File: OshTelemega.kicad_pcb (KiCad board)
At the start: 4 copper layers, 30 x 80 mm, 157 parts, among them J1 TAGCONNECT, J10 SERVOS, J2 Conn_01x02, J3 SMA_Edgelaunch, J4 USB_C_Receptacle_USB2.0_16P, J5 UFL, J6 RIGHT, J7 LEFT, J8 BATT, J9 Conn_02x05_Counter_Clockwise, Q1 SiA449DJ, Q2 AO3400A, Q3 SiA449DJ, Q4 SiA449DJ, U1 STM32L151VCTx, U10 MMC5983MA, U11 TSM200N03, U12 LM293QT, U13 LM293QT, U14 TSM200N03, U15 LM293QT, U16 TSM200N03, U17 MCP73831-2-OT, U18 TC2185-3.3VxCTTR, U19 W25Q64JVXGIQ, U2 WE-TVS-82400102, U21 SN74LVC1G80QDCKTQ1, U3 ADXL375, U4 MS5607-02BA, U5 MAX-M10S, U6 MCP130-xxxxTT, U7 DRV5012AEDMRR, U8 CC1200, U9 BMI088, X2 ECS-160-8-36Q-AES-TR1, Y1 ABM8W-40.0000MHZ

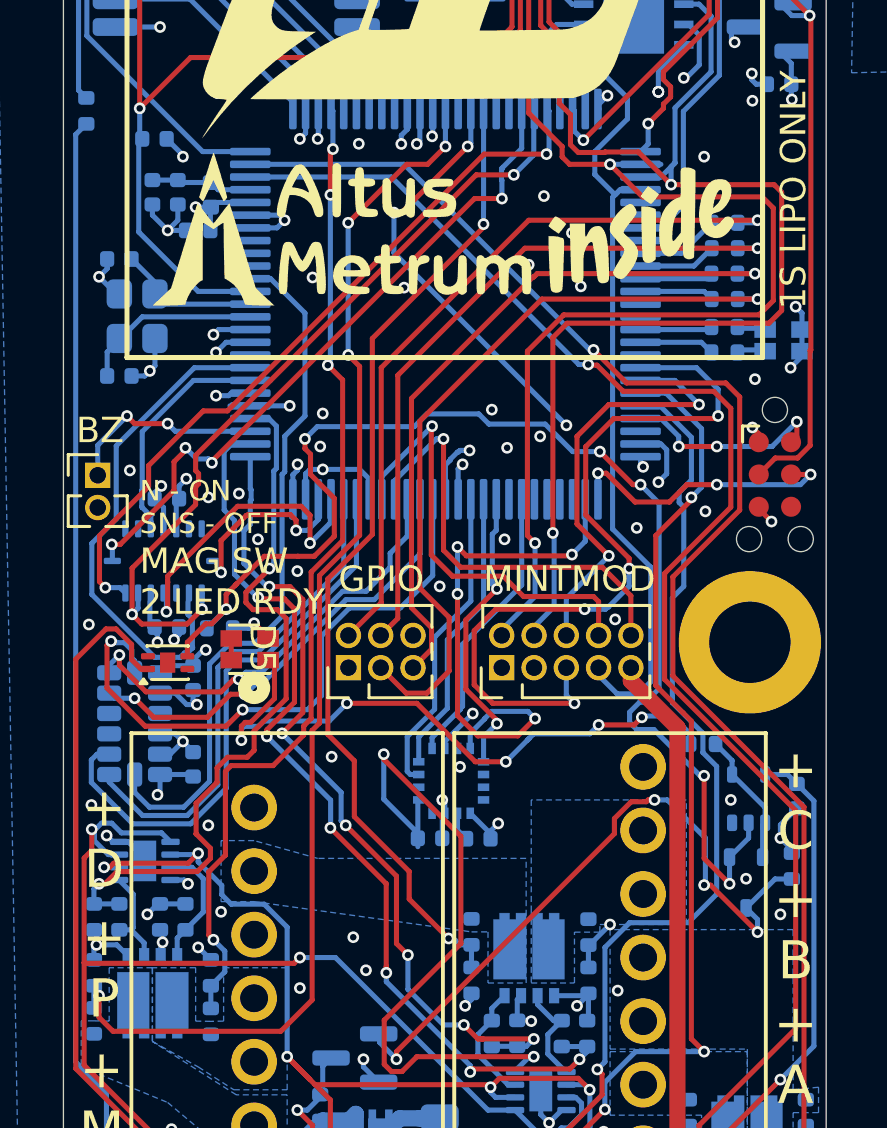
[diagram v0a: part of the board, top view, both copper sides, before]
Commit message: finished silkscreen edits. Switching branches to work on JLC DRC
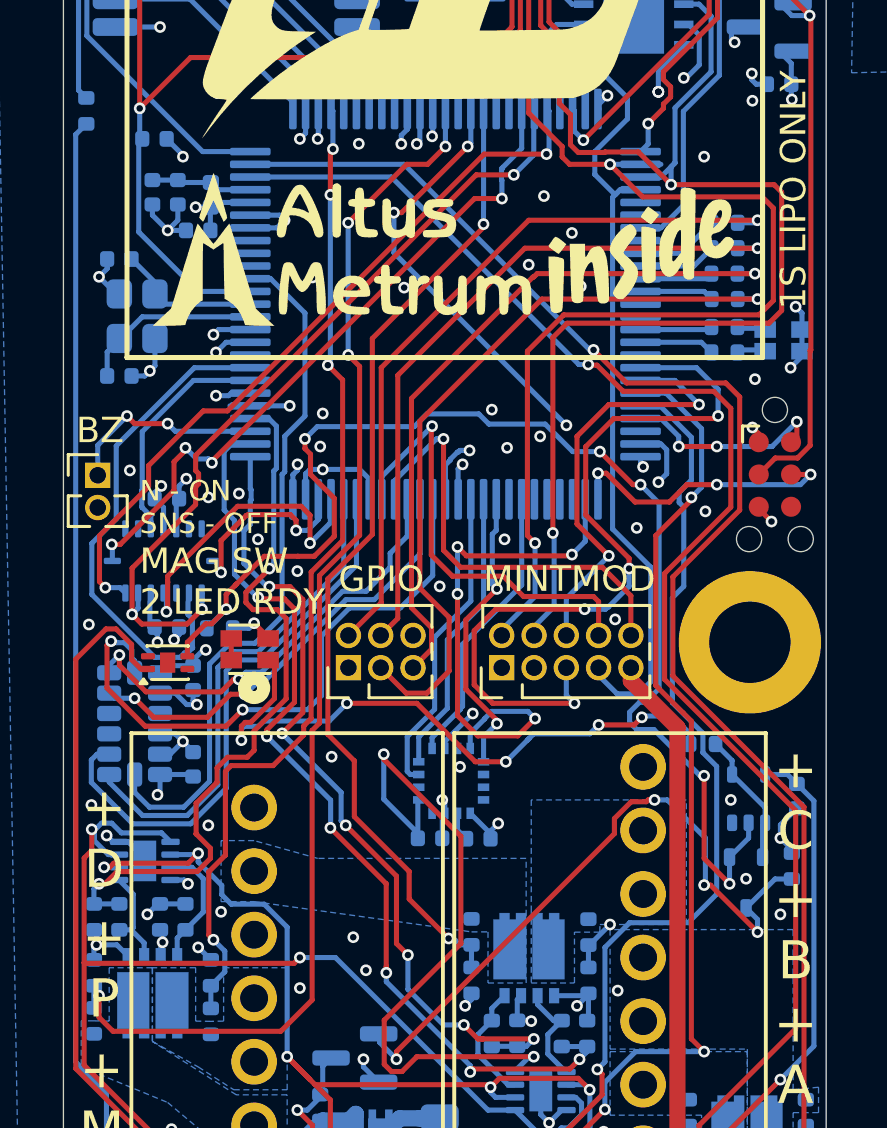
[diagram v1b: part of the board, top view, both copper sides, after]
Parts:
- added G***: LOGO, LOGO, B.Cu at (32.0, 76.8)
- moved G*** 0.80 mm to (35.0, 49.8)
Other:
- board text added: "you like rockets don't you"

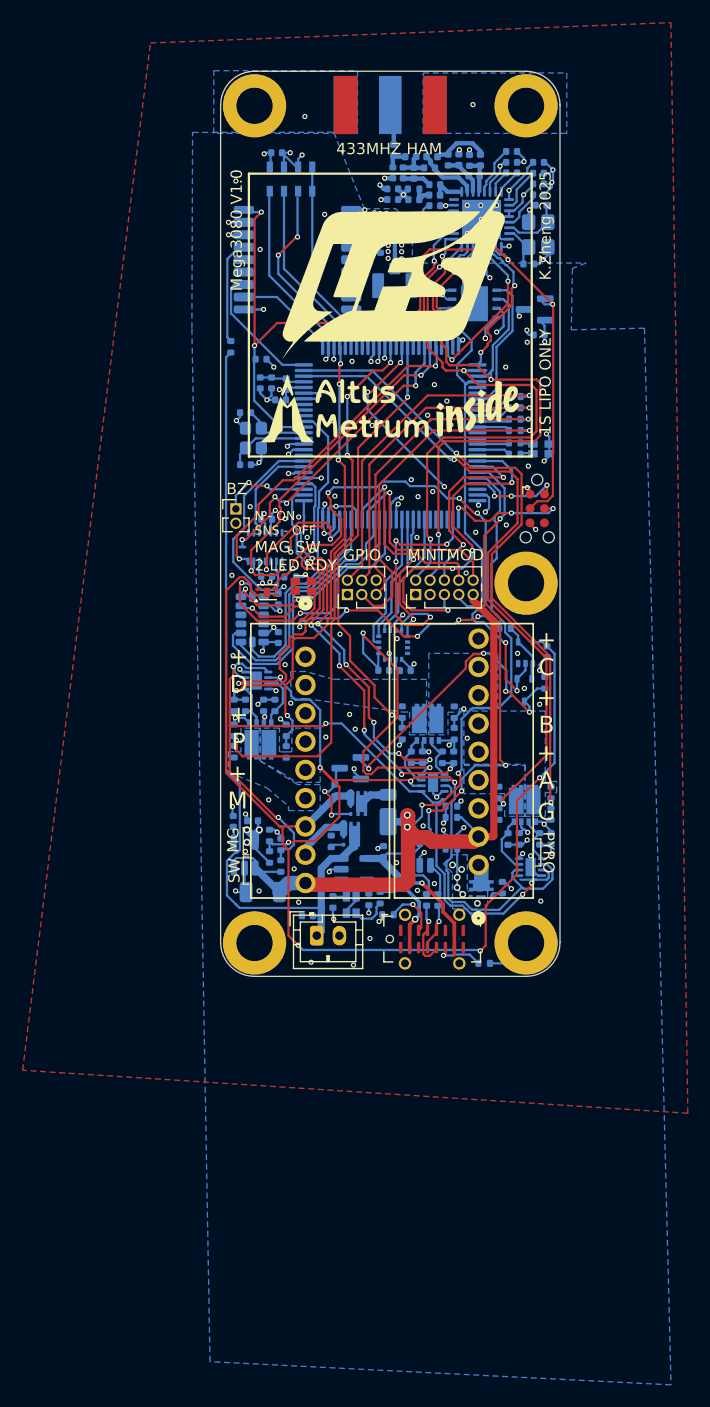
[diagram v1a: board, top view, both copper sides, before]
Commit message: drc changes and more ground stitching
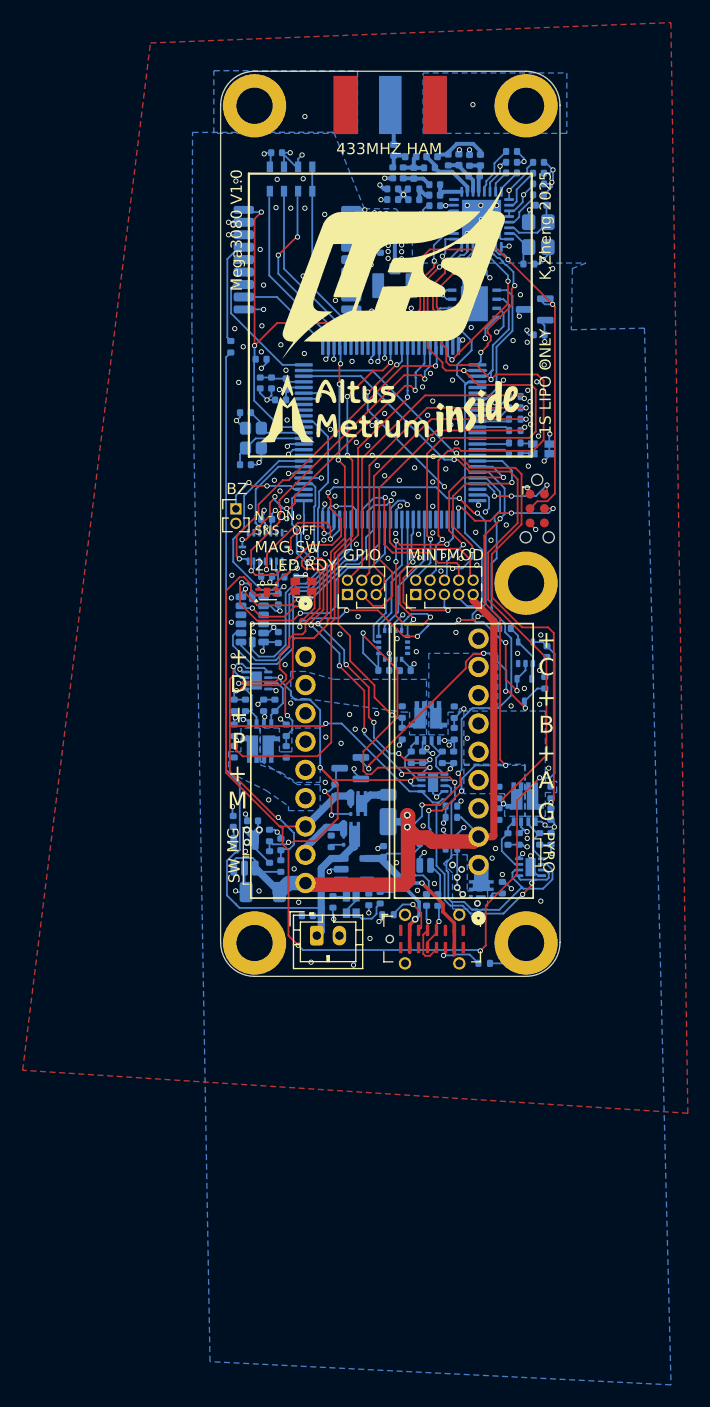
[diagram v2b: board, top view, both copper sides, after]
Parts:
- removed U11, U14, U16: TSM200N03, FCU2025Lib:8-PDFN (3x3)
- added U20: SISB46DN, FCU2025Lib:PowerPak1212-8-Dual, B.Cu at (46.9, 85.0)
- added U22: SISB46DN, FCU2025Lib:PowerPak1212-8-Dual, B.Cu at (38.3, 77.8)
- added U23: SISB46DN, FCU2025Lib:PowerPak1212-8-Dual, B.Cu at (23.5, 78.9)
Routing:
- net /SENSE_B: track 56.7 -> 58.3 mm
- net /SCK1: track 26.9 -> 28.3 mm
- net /CS_COMP1: track 17.7 -> 16.5 mm
- net /MISO2: track 58.6 -> 59.7 mm
- net Net-(Q2-G): track 26.8 -> 25.8 mm
- net /CS_COMP0: track 17.7 -> 16.9 mm
- net /MISO1: track 32.1 -> 32.8 mm
- net Net-(J10-Pin_3): track 29.8 -> 29.2 mm
- net Net-(J10-Pin_4): track 27.5 -> 26.9 mm
- net Net-(J3-In): track 4.28 -> 3.62 mm
- net Net-(J10-Pin_2): track 29.1 -> 28.5 mm
- net /MGSW_IN: track 94.3 -> 94.8 mm
- net GND: track 123.8 -> 123.4 mm, vias 151 -> 235

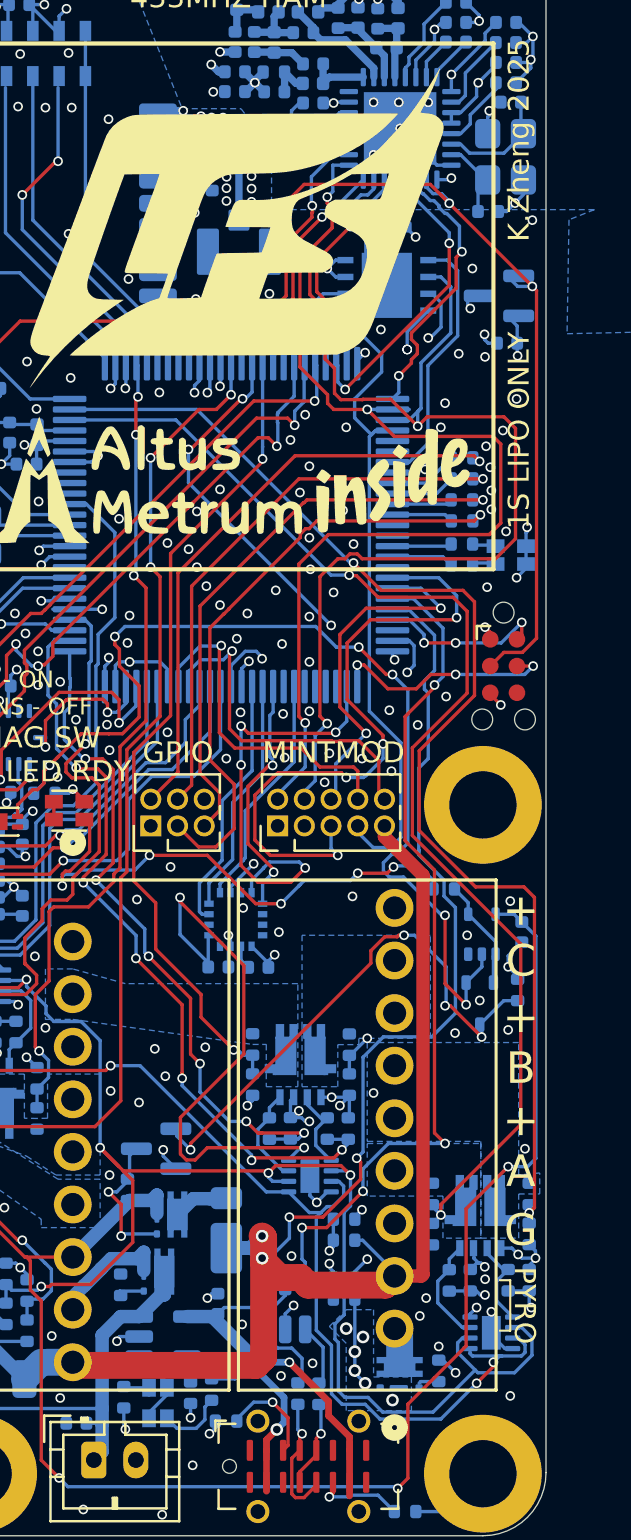
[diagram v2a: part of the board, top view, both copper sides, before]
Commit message: minor impedance tune due to new pour clearance
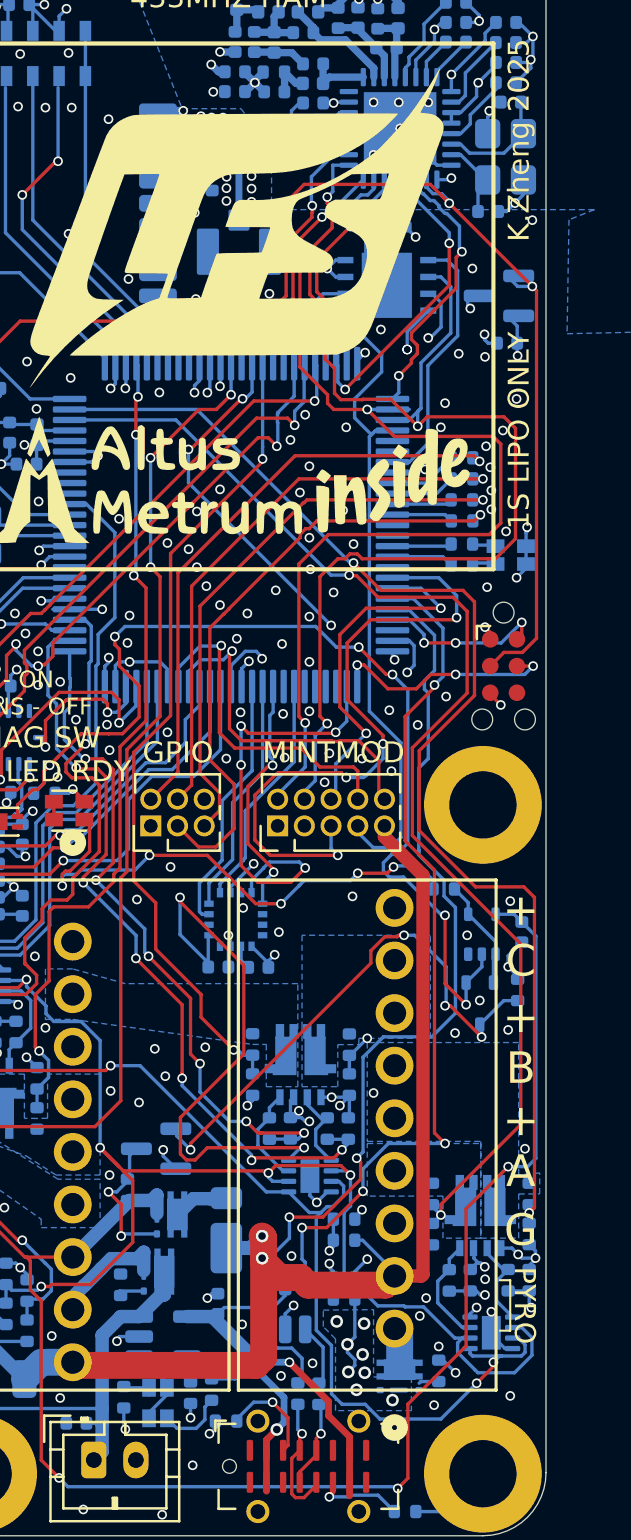
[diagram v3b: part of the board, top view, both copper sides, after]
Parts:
- moved Q4 0.12 mm to (43.0, 92.4)
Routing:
- net /CMP_RAIL: track 69.5 -> 63.7 mm
- net V_PYRO: track 4.20 -> 3.88 mm, vias 6 -> 8
- net GND: vias 235 -> 236
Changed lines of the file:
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@@
 	(footprint "Package_TO_SOT_SMD:Vishay_PowerPAK_SC70-6L_Single"
 		(layer "B.Cu")
-		(at 43.04 92.25 180)
+		(at 43.04 92.375 180)
 		(descr "Vishay PowerPAK SC70 single transistor package http://www.vishay.com/docs/70486/70486.pdf")
 		(tags "powerpak sc70 sc-70")
@@
 	)
 	(via
+		(at 44.68 93.74)
+		(size 0.46)
+		(drill 0.3)
+		(layers "F.Cu" "B.Cu")
+		(net 2)
+	)
+	(via
 		(at 36 35.3)
 		(size 0.46)
@@
 	)
 	(segment
-		(start 33.2 34.085)
-		(end 33.2 34.980002)
-		(width 0.3493)
-		(layer "B.Cu")
-		(net 35)
-	)
-	(segment
 		(start 34.076395 34.980002)
 		(end 34.128426 35.032033)
@@
 	(segment
 		(start 33.2 34.980002)
-		(end 34.076395 34.980002)
-		(width 0.3493)
+		(end 33.2 34.085)
+		(width 0.33)
 		(layer "B.Cu")
 		(net 35)
@@
 		(start 33.252031 35.032033)
 		(end 33.2 34.980002)
-		(width 0.364)
+		(width 0.33)
+		(layer "B.Cu")
+		(net 35)
+	)
+	(segment
+		(start 34.128426 35.032033)
+		(end 33.252031 35.032033)
+		(width 0.33)
 		(layer "B.Cu")
 		(net 35)
@@
 	)
 	(via
-		(at 40.91 92.1)
+		(at 40.56 90.85)
 		(size 0.6)
 		(drill 0.36)
@@
 	)
 	(via
-		(at 40.5 90.1)
+		(at 40.05 89.76)
 		(size 0.6)
 		(drill 0.36)
@@
 	)
 	(via
-		(at 41.4 92.7)
+		(at 40.6 92.16)
+		(size 0.6)
+		(drill 0.36)
+		(layers "F.Cu" "B.Cu")
+		(net 45)
+	)
+	(via
+		(at 41.28 91.33)
+		(size 0.6)
+		(drill 0.36)
+		(layers "F.Cu" "B.Cu")
+		(net 45)
+	)
+	(via
+		(at 41.38 92.2)
 		(size 0.6)
 		(drill 0.36)
@@
 	)
 	(via
-		(at 40.91 91.2)
+		(at 41.35 89.86)
 		(size 0.6)
 		(drill 0.36)
@@
 	)
 	(via
-		(at 41.3 90.5)
+		(at 40.99 93.01)
 		(size 0.6)
 		(drill 0.36)
@@
 	)
 	(segment
-		(start 40.91 92.1)
-		(end 40.91 92.21)
+		(start 40.56 90.85)
+		(end 40.91 90.5)
 		(width 0.16)
 		(layer "B.Cu")
@@
 	)
 	(segment
-		(start 40.91 92.21)
-		(end 41.4 92.7)
+		(start 40.56 91.23)
+		(end 40.91 91.58)
 		(width 0.16)
 		(layer "B.Cu")
@@
 	)
 	(segment
-		(start 40.91 88.7)
-		(end 40.91 92.1)
+		(start 40.91 91.58)
+		(end 40.91 91.85)
+		(width 0.16)
+		(layer "B.Cu")
+		(net 45)
+	)
+	(segment
+		(start 40.91 91.85)
+		(end 40.6 92.16)
+		(width 0.16)
+		(layer "B.Cu")
+		(net 45)
+	)
+	(segment
+		(start 40.56 90.85)
+		(end 40.56 91.23)
+		(width 0.16)
+		(layer "B.Cu")
+		(net 45)
+	)
+	(segment
+		(start 40.91 90.5)
+		(end 40.91 88.7)
 		(width 0.16)
 		(layer "B.Cu")
@@
 	)
 	(segment
-		(start 27.895232 75.5)
-		(end 26.6 75.5)
+		(start 43.297767 89.069)
+		(end 43.247765 89.018998)
 		(width 0.16)
 		(layer "B.Cu")
@@
 	)
 	(segment
-		(start 37 83.1)
-		(end 37.7625 83.1)
+		(start 27.895232 75.5)
+		(end 26.6 75.5)
 		(width 0.16)
 		(layer "B.Cu")
@@
 	)
 	(segment
-		(start 39.965 89.878395)
-		(end 40.4 89.443395)
+		(start 37 83.1)
+		(end 37.7625 83.1)
 		(width 0.16)
 		(layer "B.Cu")
@@
 	)
 	(segment
-		(start 40.435862 93.372)
-		(end 40.128 93.064138)
-		(width 0.16)
-		(layer "B.Cu")
-		(net 80)
-	)
-	(segment
-		(start 42.236121 94.072)
-		(end 41.536121 93.372)
-		(width 0.16)
-		(layer "B.Cu")
-		(net 80)
-	)
-	(segment
-		(start 41.536121 93.372)
-		(end 40.435862 93.372)
+		(start 43.247765 89.018998)
+		(end 41.99963 89.018998)
 		(width 0.16)
 		(layer "B.Cu")
@@
 	)
 	(segment
-		(start 40.4 89.443395)
+		(start 40.4 88.24)
 		(end 40.4 84.5729)
 		(width 0.16)
@@
 	)
 	(segment
-		(start 39.965 90.601138)
-		(end 39.965 89.878395)
-		(width 0.16)
-		(layer "B.Cu")
-		(net 80)
-	)
-	(segment
 		(start 28.8 81.5)
 		(end 28.8 76.404768)
@@
 	)
 	(segment
-		(start 44.628 94.072)
-		(end 42.236121 94.072)
+		(start 46.3875 90.55)
+		(end 45.659527 90.55)
 		(width 0.16)
 		(layer "B.Cu")
@@
 	)
 	(segment
-		(start 46.631219 92.068781)
-		(end 44.628 94.072)
-		(width 0.16)
-		(layer "B.Cu")
-		(net 80)
-	)
-	(segment
 		(start 48.501425 92.2)
 		(end 46.762438 92.2)
@@
 	)
 	(segment
+		(start 41.180632 88.2)
+		(end 40.44 88.2)
+		(width 0.16)
+		(layer "B.Cu")
+		(net 80)
+	)
+	(segment
 		(start 40.7 82.8)
 		(end 40.5 82.6)
@@
 	)
 	(segment
-		(start 40.128 90.764138)
-		(end 39.965 90.601138)
+		(start 49.331001 90.531001)
+		(end 49.331001 91.370424)
 		(width 0.16)
 		(layer "B.Cu")
@@
 	)
 	(segment
-		(start 49.331001 90.531001)
-		(end 49.331001 91.370424)
+		(start 40.44 88.2)
+		(end 40.4 88.24)
 		(width 0.16)
 		(layer "B.Cu")
@@
 	)
 	(segment
-		(start 40.128 93.064138)
-		(end 40.128 90.764138)
+		(start 45.659527 90.55)
+		(end 44.178527 89.069)
 		(width 0.16)
 		(layer "B.Cu")
@@
 	)
 	(segment
+		(start 44.178527 89.069)
+		(end 43.297767 89.069)
+		(width 0.16)
+		(layer "B.Cu")
+		(net 80)
+	)
+	(segment
+		(start 41.99963 89.018998)
+		(end 41.180632 88.2)
+		(width 0.16)
+		(layer "B.Cu")
+		(net 80)
+	)
+	(segment
 		(start 26.228 75.128)
 		(end 26.228 74.764138)
@@
 		(start 32.6 36.6)
 		(end 31.55 36.6)
-		(width 0.3493)
+		(width 0.33)
 		(layer "B.Cu")
 		(net 148)
@@
 		(start 33.2 36)
 		(end 32.6 36.6)
-		(width 0.3493)
+		(width 0.33)
 		(layer "B.Cu")
 		(net 148)
@@
 	)
 	(segment
-		(start 34.489867 33.115)
-		(end 35.4 34.025133)
-		(width 0.3493)
-		(layer "B.Cu")
-		(net 163)
-	)
-	(segment
-		(start 31.55 33.3)
-		(end 33.015 33.3)
-		(width 0.3493)
+		(start 33.2 33.115)
+		(end 31.735 33.115)
+		(width 0.33)
 		(layer "B.Cu")
 		(net 163)
 	)
 	(segment
-		(start 35.4 34.025133)
-		(end 35.4 37.4)
-		(width 0.3493)
+		(start 31.735 33.115)
+		(end 31.55 33.3)
+		(width 0.33)
 		(layer "B.Cu")
 		(net 163)
 	)
 	(segment
-		(start 33.2 33.115)
-		(end 34.489867 33.115)
-		(width 0.3493)
+		(start 34.595 33.115)
+		(end 35.4 33.92)
+		(width 0.33)
 		(layer "B.Cu")
 		(net 163)
 	)
 	(segment
-		(start 33.015 33.3)
-		(end 33.2 33.115)
-		(width 0.3493)
+		(start 31.55 33.3)
+		(end 31.649999 33.399999)
+		(width 0.3686)
 		(layer "B.Cu")
 		(net 163)
 	)
 	(segment
-		(start 31.55 33.3)
-		(end 31.649999 33.399999)
-		(width 0.3686)
+		(start 33.2 33.115)
+		(end 34.595 33.115)
+		(width 0.33)
 		(layer "B.Cu")
 		(net 163)
 	)
 	(segment
-		(start 31.735 33.115)
-		(end 31.55 33.3)
-		(width 0.364)
+		(start 35.4 33.92)
+		(end 35.4 37.4)
+		(width 0.33)
 		(layer "B.Cu")
 		(net 163)
@@
 		(polygon
 			(pts
-				(xy 40.5 90.8) (xy 39.7 90) (xy 40.5 89.2) (xy 41.8 89.2) (xy 41.8 92.4) (xy 43.6 92.4) (xy 43.6 94)
-				(xy 40.5 94)
+				(xy 39.99 90.59) (xy 39.41 90.01) (xy 39.41 89.222762) (xy 41.8 89.2) (xy 41.8 92.4) (xy 43.6 92.4)
+				(xy 43.6 94) (xy 39.99 94)
 			)
 		)
